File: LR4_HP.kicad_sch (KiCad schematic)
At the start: 13 parts, among them U8 TL072

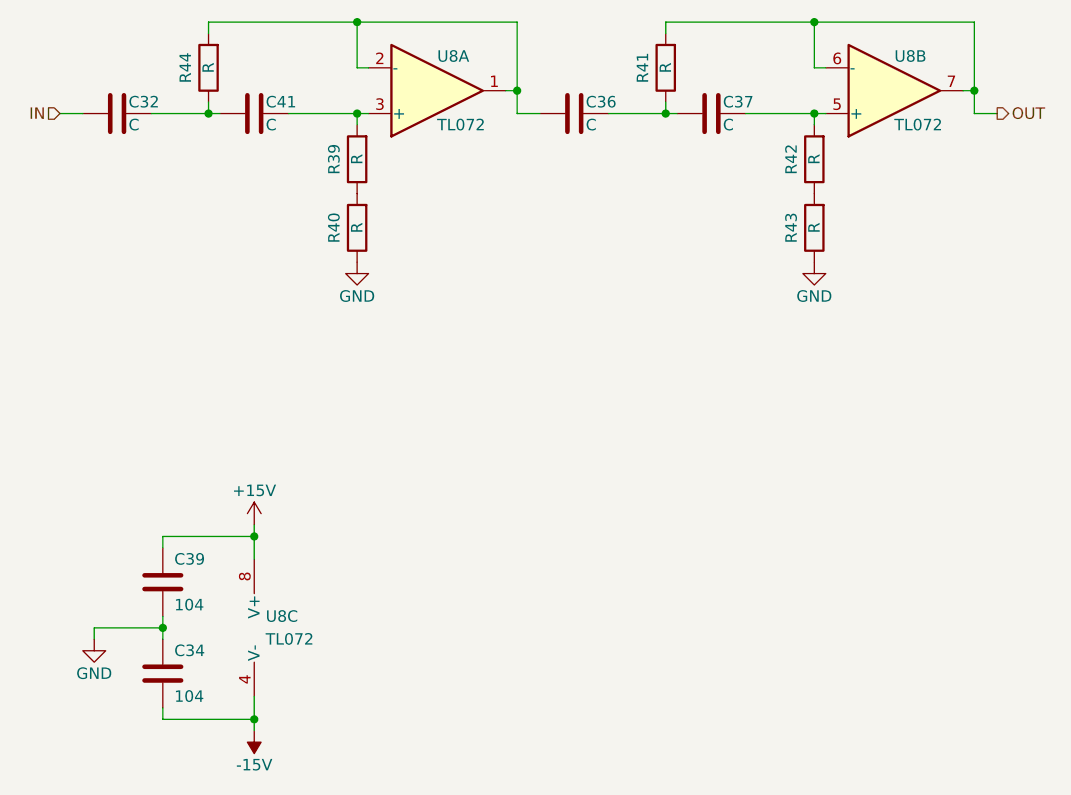
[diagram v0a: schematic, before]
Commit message: Added XLR input connectors for direct panel mounting. Added snap-off board for the level control pots with ribbon cable connection to the main board.
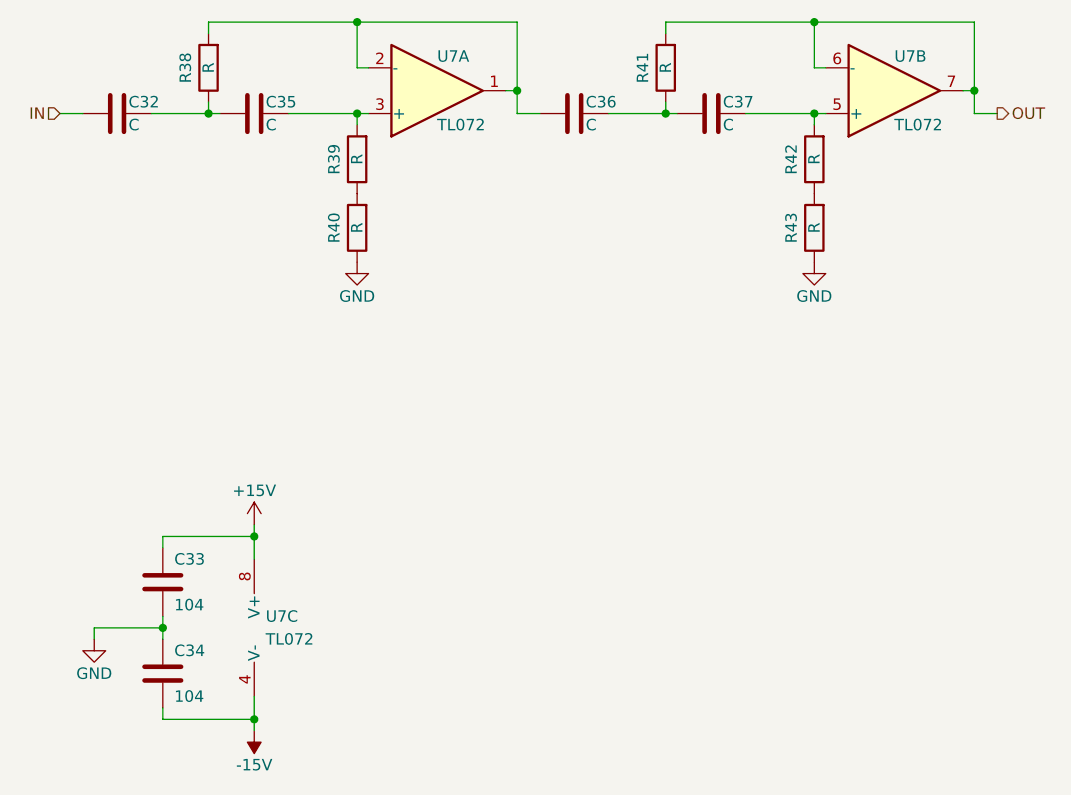
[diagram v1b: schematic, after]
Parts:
- renumbered C39 to C33, C41 to C35, R44 to R38, U8 to U7
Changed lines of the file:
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@@
 		(on_board yes)
 		(dnp no)
-		(property "Reference" "U8"
+		(property "Reference" "U7"
 			(at 109.22 69.85 0)
 			(effects
@@
 		(on_board yes)
 		(dnp no)
-		(property "Reference" "C39"
+		(property "Reference" "C33"
 			(at 80.01 125.73 0)
 			(effects
@@
 		(on_board yes)
 		(dnp no)
-		(property "Reference" "#PWR040"
+		(property "Reference" "#PWR035"
 			(at 88.9 125.73 0)
 			(effects
@@
 		(on_board yes)
 		(dnp no)
-		(property "Reference" "#PWR041"
+		(property "Reference" "#PWR036"
 			(at 88.9 140.97 0)
 			(effects
@@
 		(on_board yes)
 		(dnp no)
-		(property "Reference" "#PWR043"
+		(property "Reference" "#PWR038"
 			(at 151.13 99.06 0)
 			(effects
@@
 		(dnp no)
 		(fields_autoplaced yes)
-		(property "Reference" "U8"
+		(property "Reference" "U7"
 			(at 90.17 132.0799 0)
 			(effects
@@
 		(on_board yes)
 		(dnp no)
-		(property "Reference" "U8"
+		(property "Reference" "U7"
 			(at 160.02 69.85 0)
 			(effects
@@
 		(on_board yes)
 		(dnp no)
-		(property "Reference" "R44"
+		(property "Reference" "R38"
 			(at 81.28 71.12 90)
 			(effects
@@
 		(on_board yes)
 		(dnp no)
-		(property "Reference" "#PWR042"
+		(property "Reference" "#PWR037"
 			(at 100.33 99.06 0)
 			(effects
@@
 		(on_board yes)
 		(dnp no)
-		(property "Reference" "C41"
+		(property "Reference" "C35"
 			(at 90.17 74.93 90)
 			(effects
